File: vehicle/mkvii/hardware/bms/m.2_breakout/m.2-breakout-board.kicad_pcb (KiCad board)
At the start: 2 copper layers, 30 x 76.5 mm, 84 parts, among them J1 Pin_Header_1, J2 Pin_Header_2, J3 Automotive_M.2_Edge_Connector, J4 Automotive_M.2

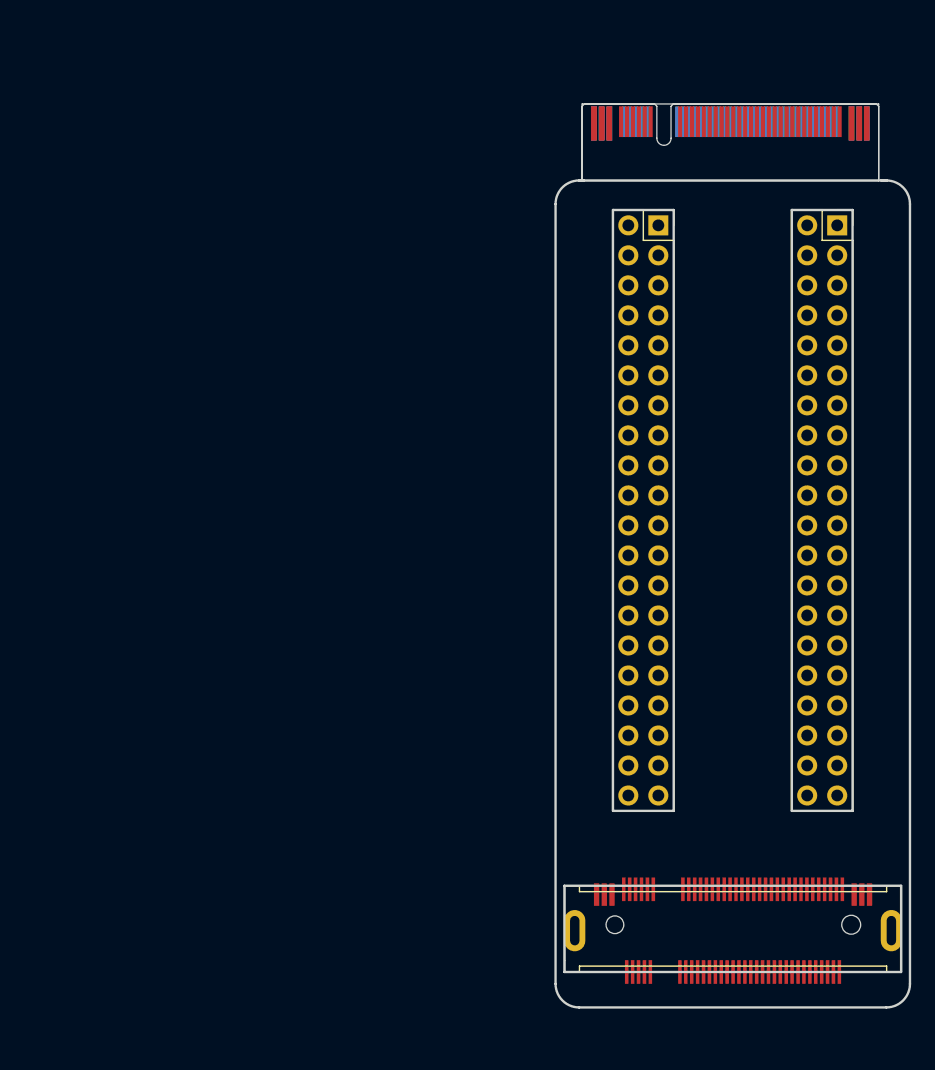
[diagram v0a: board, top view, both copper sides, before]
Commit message: Update of m.2 breakout board layout and schematic
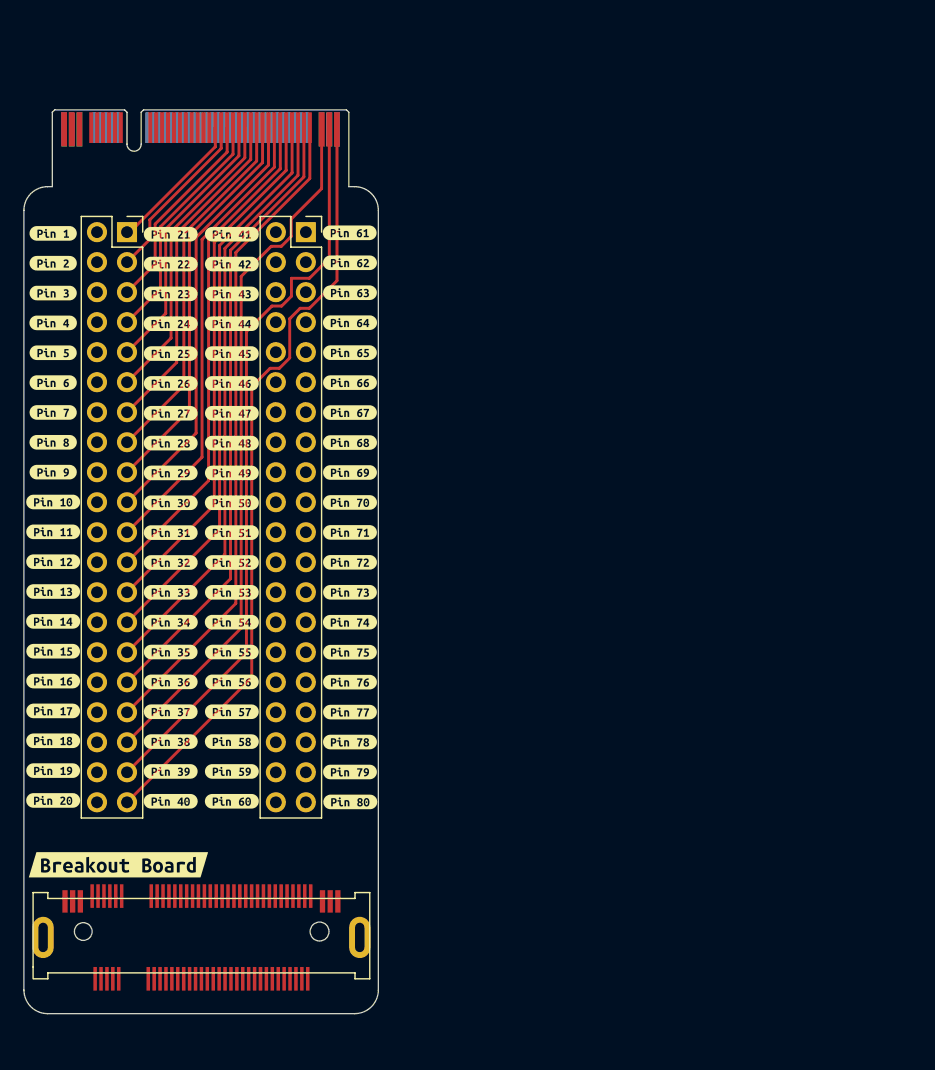
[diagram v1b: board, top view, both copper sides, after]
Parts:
- removed kibuzzard-65E4BBCA (x80): G***, kibuzzard-65E4BBCA
- added kibuzzard-65E4F8A3: G***, kibuzzard-65E4F8A3, F.Cu at (134.8, 109.7)
- added kibuzzard-65E4F8A7: G***, kibuzzard-65E4F8A7, F.Cu at (134.8, 107.2)
- added kibuzzard-65E4F8AD: G***, kibuzzard-65E4F8AD, F.Cu at (134.8, 104.6)
- added kibuzzard-65E4F907: G***, kibuzzard-65E4F907, F.Cu at (134.8, 102.1)
- added kibuzzard-65E4F90C: G***, kibuzzard-65E4F90C, F.Cu at (134.8, 99.6)
- added kibuzzard-65E4F911: G***, kibuzzard-65E4F911, F.Cu at (134.8, 97.1)
- added kibuzzard-65E4F916: G***, kibuzzard-65E4F916, F.Cu at (134.8, 94.5)
- added kibuzzard-65E4F928: G***, kibuzzard-65E4F928, F.Cu at (134.8, 92.0)
- added kibuzzard-65E4F92D: G***, kibuzzard-65E4F92D, F.Cu at (134.8, 89.5)
- added kibuzzard-65E4F932: G***, kibuzzard-65E4F932, F.Cu at (134.8, 87.0)
- added kibuzzard-65E4F936: G***, kibuzzard-65E4F936, F.Cu at (134.8, 84.4)
- added kibuzzard-65E4F93A: G***, kibuzzard-65E4F93A, F.Cu at (134.8, 81.9)
- added kibuzzard-65E4F941: G***, kibuzzard-65E4F941, F.Cu at (134.8, 79.4)
- added kibuzzard-65E4F946: G***, kibuzzard-65E4F946, F.Cu at (134.8, 76.9)
- added kibuzzard-65E4F94A: G***, kibuzzard-65E4F94A, F.Cu at (129.7, 76.8)
- added kibuzzard-65E4F951: G***, kibuzzard-65E4F951, F.Cu at (129.7, 79.4)
- added kibuzzard-65E4F955: G***, kibuzzard-65E4F955, F.Cu at (129.7, 81.9)
- added kibuzzard-65E4F95B: G***, kibuzzard-65E4F95B, F.Cu at (129.7, 84.4)
- added kibuzzard-65E4F960: G***, kibuzzard-65E4F960, F.Cu at (129.7, 87.0)
- added kibuzzard-65E4F96C: G***, kibuzzard-65E4F96C, F.Cu at (129.7, 89.5)
- added kibuzzard-65E4F97B: G***, kibuzzard-65E4F97B, F.Cu at (129.7, 92.0)
- added kibuzzard-65E4F981: G***, kibuzzard-65E4F981, F.Cu at (129.7, 94.5)
- added kibuzzard-65E4F987: G***, kibuzzard-65E4F987, F.Cu at (129.7, 97.1)
- added kibuzzard-65E4F98D: G***, kibuzzard-65E4F98D, F.Cu at (129.7, 99.6)
- added kibuzzard-65E4F991: G***, kibuzzard-65E4F991, F.Cu at (129.7, 102.1)
- added kibuzzard-65E4F997: G***, kibuzzard-65E4F997, F.Cu at (129.7, 104.6)
- added kibuzzard-65E4F99B: G***, kibuzzard-65E4F99B, F.Cu at (129.7, 107.2)
- added kibuzzard-65E4F9A4: G***, kibuzzard-65E4F9A4, F.Cu at (129.7, 109.7)
- added kibuzzard-65E4F9A9: G***, kibuzzard-65E4F9A9, F.Cu at (129.7, 112.2)
- added kibuzzard-65E4F9B0: G***, kibuzzard-65E4F9B0, F.Cu at (129.7, 114.7)
- added kibuzzard-65E4F9B6: G***, kibuzzard-65E4F9B6, F.Cu at (129.7, 117.3)
- added kibuzzard-65E4F9CB: G***, kibuzzard-65E4F9CB, F.Cu at (129.7, 119.8)
- added kibuzzard-65E4F9F7: G***, kibuzzard-65E4F9F7, F.Cu at (129.7, 122.3)
- added kibuzzard-65E4F9FC: G***, kibuzzard-65E4F9FC, F.Cu at (129.7, 124.8)
- added kibuzzard-65E4FA07: G***, kibuzzard-65E4FA07, F.Cu at (134.8, 112.2)
- added kibuzzard-65E4FB5F: G***, kibuzzard-65E4FB5F, F.Cu at (134.8, 114.7)
- added kibuzzard-65E4FB6A: G***, kibuzzard-65E4FB6A, F.Cu at (134.8, 117.3)
- added kibuzzard-65E4FB72: G***, kibuzzard-65E4FB72, F.Cu at (134.8, 119.8)
- added kibuzzard-65E4FB7A: G***, kibuzzard-65E4FB7A, F.Cu at (134.8, 122.3)
- added kibuzzard-65E4FB85: G***, kibuzzard-65E4FB85, F.Cu at (134.8, 124.9)
- added kibuzzard-65E4FB98: G***, kibuzzard-65E4FB98, F.Cu at (144.8, 76.7)
- added kibuzzard-65E4FBA6: G***, kibuzzard-65E4FBA6, F.Cu at (144.8, 79.3)
- added kibuzzard-65E4FBAD: G***, kibuzzard-65E4FBAD, F.Cu at (144.8, 81.8)
- added kibuzzard-65E4FBB5: G***, kibuzzard-65E4FBB5, F.Cu at (144.8, 84.3)
- added kibuzzard-65E4FBBB: G***, kibuzzard-65E4FBBB, F.Cu at (144.8, 86.9)
- added kibuzzard-65E4FBCB: G***, kibuzzard-65E4FBCB, F.Cu at (144.8, 89.4)
- added kibuzzard-65E4FBD4: G***, kibuzzard-65E4FBD4, F.Cu at (144.8, 91.9)
- added kibuzzard-65E4FBDC: G***, kibuzzard-65E4FBDC, F.Cu at (144.8, 94.5)
- added kibuzzard-65E4FBE5: G***, kibuzzard-65E4FBE5, F.Cu at (144.8, 97.0)
- added kibuzzard-65E4FBEC: G***, kibuzzard-65E4FBEC, F.Cu at (144.8, 99.6)
- added kibuzzard-65E4FBF3: G***, kibuzzard-65E4FBF3, F.Cu at (144.8, 102.1)
- added kibuzzard-65E4FC00: G***, kibuzzard-65E4FC00, F.Cu at (144.8, 104.6)
- added kibuzzard-65E4FC08: G***, kibuzzard-65E4FC08, F.Cu at (144.8, 107.2)
- added kibuzzard-65E4FC1B: G***, kibuzzard-65E4FC1B, F.Cu at (144.8, 109.7)
- added kibuzzard-65E4FC24: G***, kibuzzard-65E4FC24, F.Cu at (144.8, 112.2)
- added kibuzzard-65E4FC2C: G***, kibuzzard-65E4FC2C, F.Cu at (144.8, 114.8)
- added kibuzzard-65E4FC33: G***, kibuzzard-65E4FC33, F.Cu at (144.8, 117.3)
- added kibuzzard-65E4FC39: G***, kibuzzard-65E4FC39, F.Cu at (144.8, 119.8)
- added kibuzzard-65E4FC40: G***, kibuzzard-65E4FC40, F.Cu at (144.8, 122.4)
- added kibuzzard-65E4FC47: G***, kibuzzard-65E4FC47, F.Cu at (144.8, 124.9)
- added kibuzzard-65E4FC55: G***, kibuzzard-65E4FC55, F.Cu at (119.7, 76.8)
- added kibuzzard-65E4FC5A: G***, kibuzzard-65E4FC5A, F.Cu at (119.7, 79.3)
- added kibuzzard-65E4FC61: G***, kibuzzard-65E4FC61, F.Cu at (119.7, 81.8)
- added kibuzzard-65E4FC65: G***, kibuzzard-65E4FC65, F.Cu at (119.7, 84.4)
- added kibuzzard-65E4FC69: G***, kibuzzard-65E4FC69, F.Cu at (119.7, 86.9)
- added kibuzzard-65E4FC6E: G***, kibuzzard-65E4FC6E, F.Cu at (119.7, 89.4)
- added kibuzzard-65E4FC72: G***, kibuzzard-65E4FC72, F.Cu at (119.7, 91.9)
- added kibuzzard-65E4FC7A: G***, kibuzzard-65E4FC7A, F.Cu at (119.7, 94.5)
- added kibuzzard-65E4FC7E: G***, kibuzzard-65E4FC7E, F.Cu at (119.7, 97.0)
- added kibuzzard-65E4FC83: G***, kibuzzard-65E4FC83, F.Cu at (119.7, 99.5)
- added kibuzzard-65E4FC86: G***, kibuzzard-65E4FC86, F.Cu at (119.7, 102.0)
- added kibuzzard-65E4FC8B: G***, kibuzzard-65E4FC8B, F.Cu at (119.7, 104.6)
- added kibuzzard-65E4FC8F: G***, kibuzzard-65E4FC8F, F.Cu at (119.7, 107.1)
- added kibuzzard-65E4FC95: G***, kibuzzard-65E4FC95, F.Cu at (119.7, 109.6)
- added kibuzzard-65E4FC9A: G***, kibuzzard-65E4FC9A, F.Cu at (119.7, 112.1)
- added kibuzzard-65E4FC9E: G***, kibuzzard-65E4FC9E, F.Cu at (119.7, 114.7)
- added kibuzzard-65E4FCA3: G***, kibuzzard-65E4FCA3, F.Cu at (119.7, 117.2)
- added kibuzzard-65E4FCA8: G***, kibuzzard-65E4FCA8, F.Cu at (119.7, 119.7)
- added kibuzzard-65E4FCAC: G***, kibuzzard-65E4FCAC, F.Cu at (119.7, 122.3)
- added kibuzzard-65E4FCB0: G***, kibuzzard-65E4FCB0, F.Cu at (119.7, 124.8)
- added kibuzzard-65E52195: G***, kibuzzard-65E52195, F.Cu at (125.2, 130.2)
- moved J4 45.0 mm to (132.2, 135.9)
- moved J1 45.0 mm to (126.0, 76.7)
- moved J2 45.0 mm to (141.1, 76.7)
- moved J3 44.9 mm to (132.2, 66.3)
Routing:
- net /40: track 0.00 -> 65.2 mm
- net /39: track 0.00 -> 62.9 mm
- net /38: track 0.00 -> 59.2 mm
- net /37: track 0.00 -> 55.9 mm
- net /36: track 0.00 -> 53.2 mm
- net /35: track 0.00 -> 50.4 mm
- net /34: track 0.00 -> 47.7 mm
- net /33: track 0.00 -> 44.9 mm
- net /32: track 0.00 -> 42.2 mm
- net /31: track 0.00 -> 39.4 mm
- net /30: track 0.00 -> 36.7 mm
- net /29: track 0.00 -> 33.9 mm
- net /28: track 0.00 -> 31.2 mm
- net /27: track 0.00 -> 28.4 mm
- net /26: track 0.00 -> 25.7 mm
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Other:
- board size 30 x 76.5 mm -> 30 x 70 mm

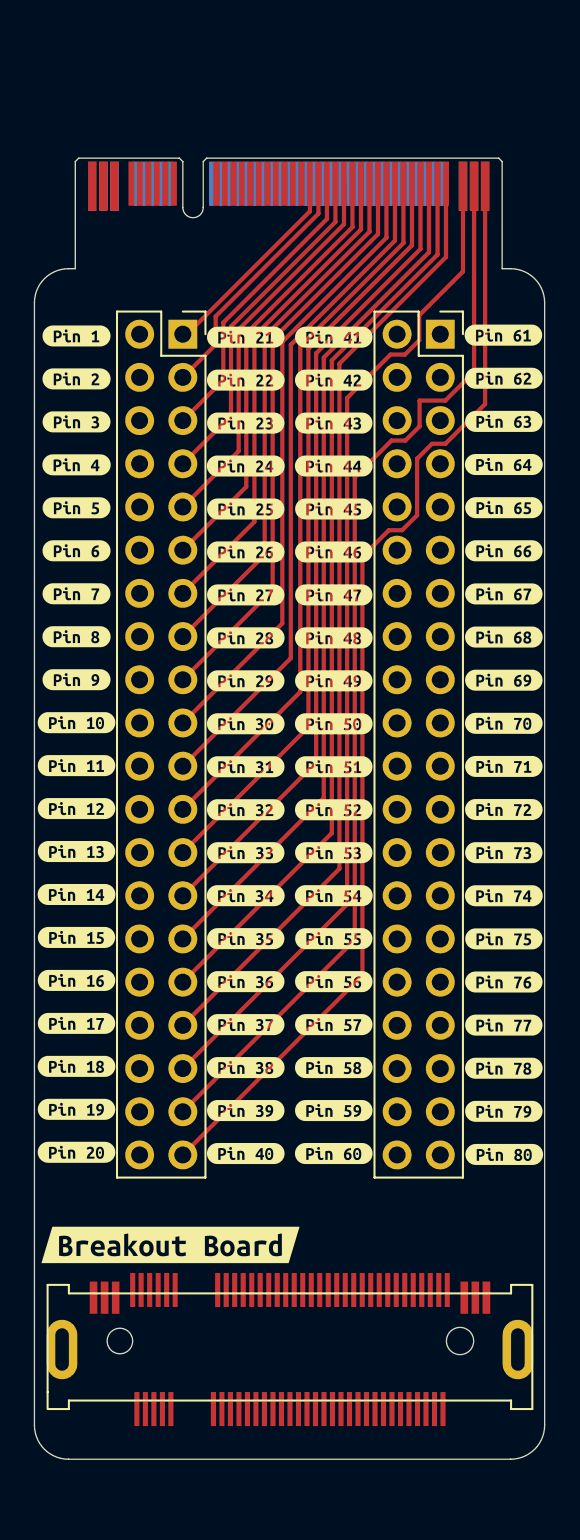
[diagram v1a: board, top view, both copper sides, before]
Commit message: Added m.2 breakout board
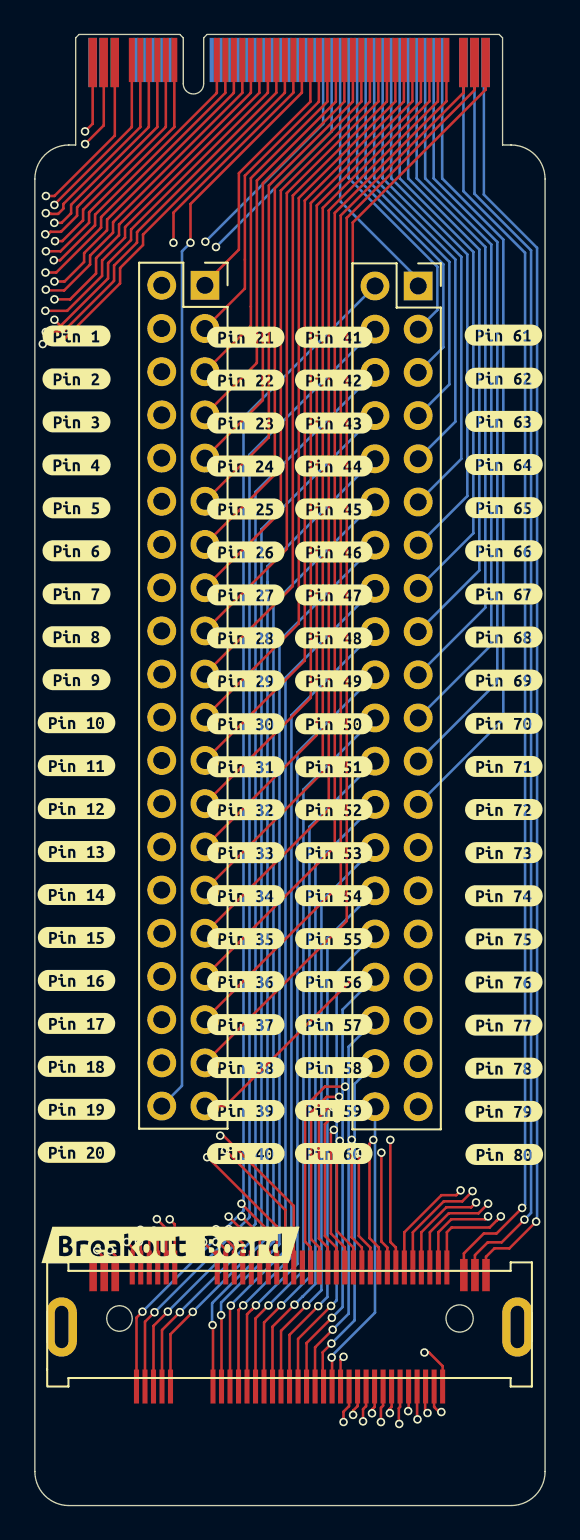
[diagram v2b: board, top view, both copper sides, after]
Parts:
- moved J3 7.28 mm to (132.2, 59.0)
- moved J1 3.16 mm to (127.2, 73.8)
- moved J2 3.12 mm to (139.8, 73.8)
- moved J4 1.33 mm to (132.2, 134.6)
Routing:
- net /38: track 59.2 -> 165.5 mm, vias 0 -> 1
- net /39: track 62.9 -> 166.0 mm, vias 0 -> 1
- net /40: track 65.2 -> 168.1 mm, vias 0 -> 1
- net /62: track 0.00 -> 101.8 mm, vias 0 -> 1
- net /63: track 0.00 -> 100.4 mm, vias 0 -> 1
- net /64: track 0.00 -> 97.6 mm, vias 0 -> 1
- net /65: track 0.00 -> 96.3 mm, vias 0 -> 1
- net /66: track 0.00 -> 95.0 mm, vias 0 -> 1
- net /68: track 0.00 -> 94.7 mm, vias 0 -> 1
- net /67: track 0.00 -> 93.7 mm, vias 0 -> 1
- net /69: track 0.00 -> 93.3 mm, vias 0 -> 1
- net /70: track 0.00 -> 91.9 mm, vias 0 -> 1
- net /71: track 0.00 -> 90.3 mm, vias 0 -> 1
- net /72: track 0.00 -> 88.4 mm, vias 0 -> 1
- net /17: track 0.00 -> 86.6 mm, vias 0 -> 2
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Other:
- board size 30 x 70 mm -> 30 x 80 mm
- copper layers 2 -> 4

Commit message: update old files
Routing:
- net /58: track 23.0 -> 87.7 mm, vias 1 -> 2
- net /57: track 25.7 -> 86.7 mm, vias 1 -> 2
- net /56: track 28.5 -> 87.7 mm, vias 1 -> 2
- net /55: track 31.2 -> 86.5 mm, vias 1 -> 2
- net /54: track 34.0 -> 87.7 mm, vias 1 -> 2
- net /59: track 33.8 -> 86.6 mm
- net /52: track 39.5 -> 90.8 mm, vias 1 -> 2
- net /51: track 42.2 -> 92.6 mm, vias 1 -> 2
- net /53: track 36.7 -> 86.7 mm, vias 1 -> 2
- net /50: track 45.0 -> 92.1 mm, vias 1 -> 2
- net /49: track 47.7 -> 94.0 mm, vias 1 -> 2
- net /48: track 50.5 -> 93.4 mm, vias 1 -> 2
- net /47: track 53.2 -> 95.0 mm, vias 1 -> 2
- net /46: track 56.0 -> 94.5 mm, vias 1 -> 2
- net /45: track 60.3 -> 97.1 mm, vias 1 -> 2
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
